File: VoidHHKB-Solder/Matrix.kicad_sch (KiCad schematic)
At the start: 136 parts

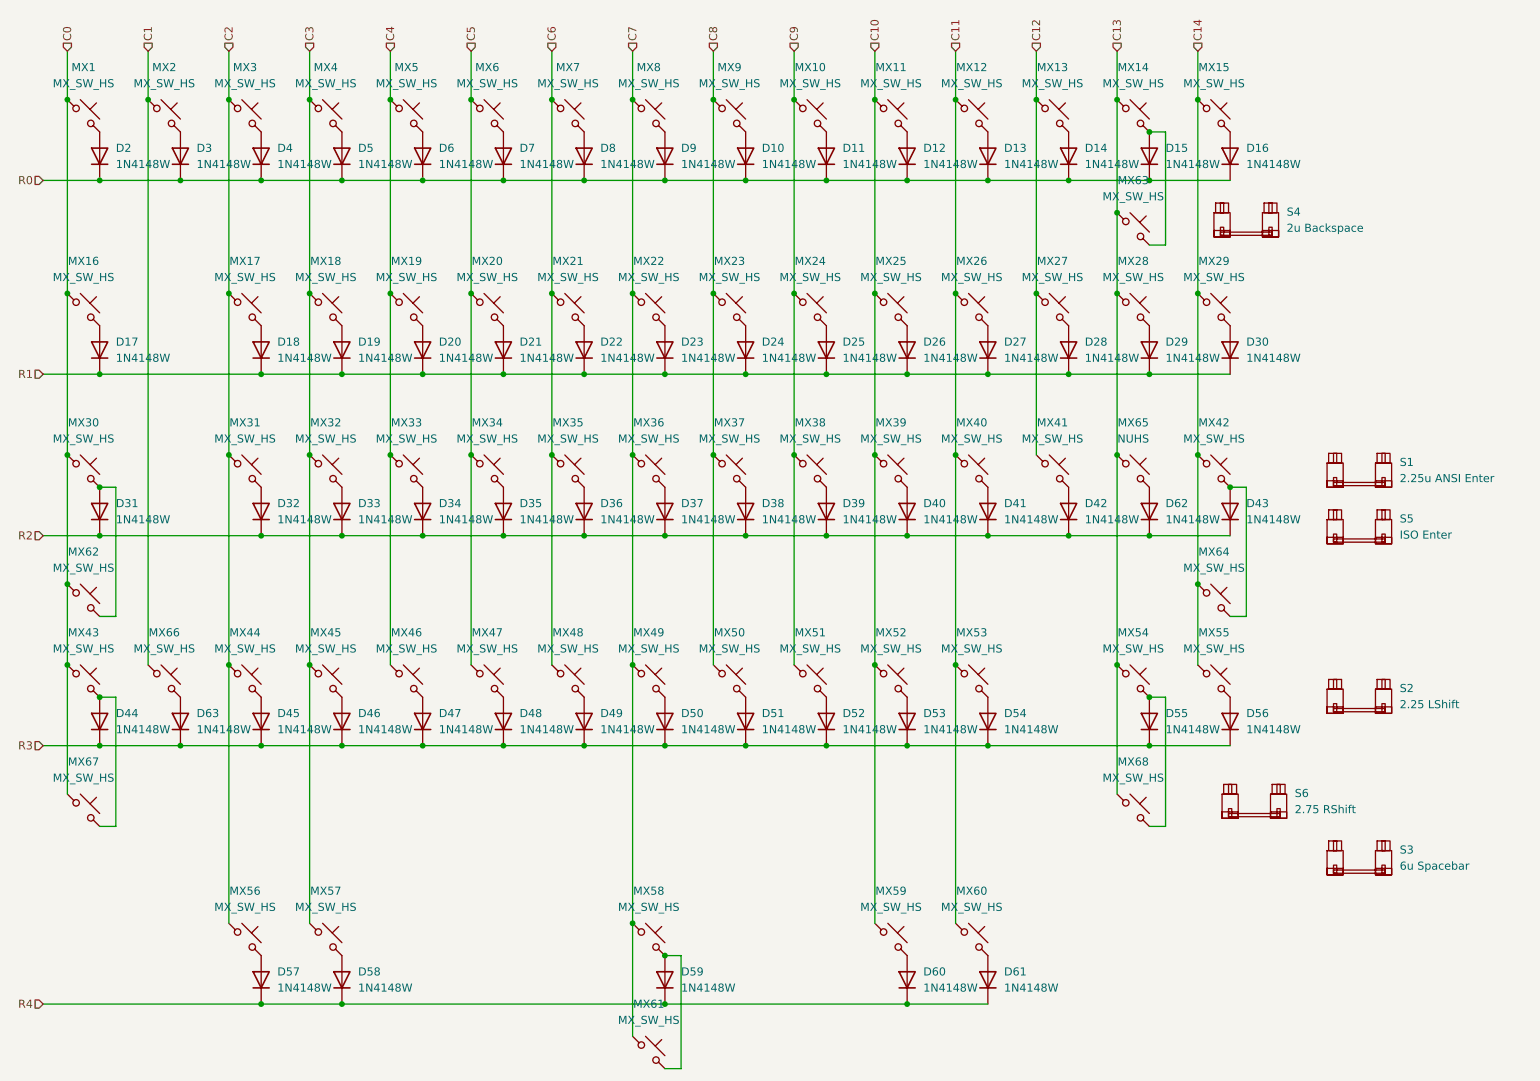
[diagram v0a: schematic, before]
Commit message: Updated Solder PCB. Fix designators and add labels to silk screen.
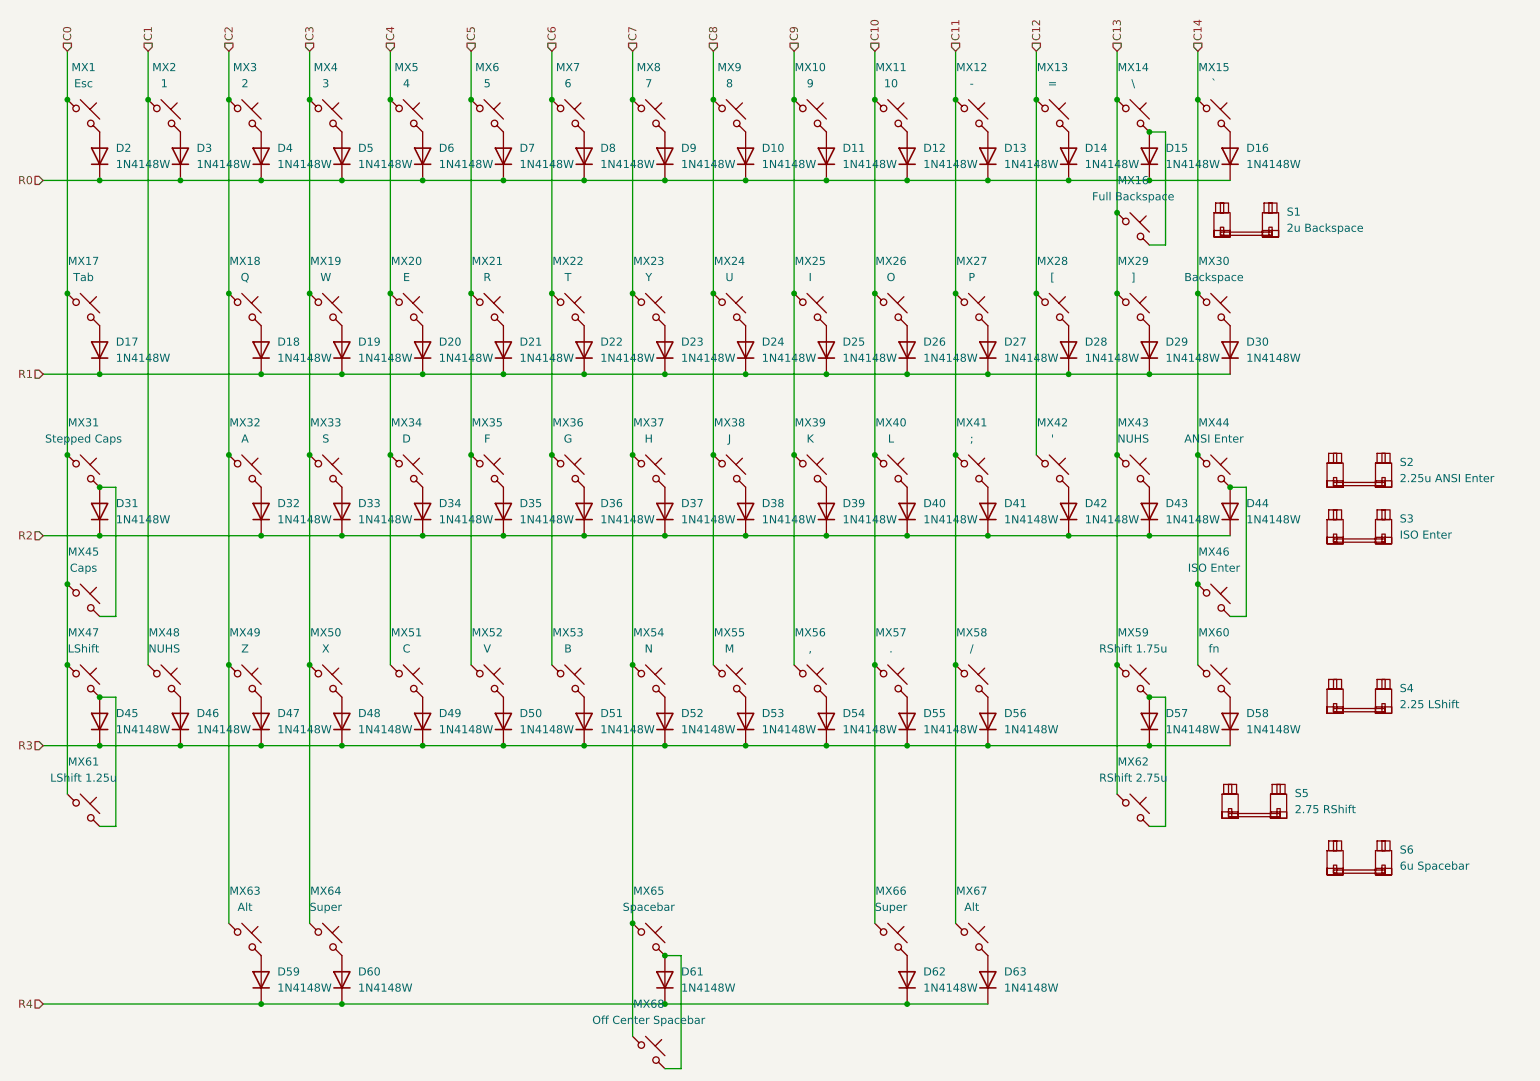
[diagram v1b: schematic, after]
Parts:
- MX1: value MX_SW_HS -> Esc
- MX10: value MX_SW_HS -> 9
- MX11: value MX_SW_HS -> 10
- MX12: value MX_SW_HS -> -
- MX13: value MX_SW_HS -> =
- MX14: value MX_SW_HS -> \
- MX15: value MX_SW_HS -> `
- MX16: renamed from MX63; value MX_SW_HS -> Full Backspace
- MX17: renamed from MX16; value MX_SW_HS -> Tab; footprint PCM_marbastlib-mx:SW_MX_1u -> PCM_marbastlib-mx:SW_MX_1.5u
- MX18: renamed from MX17; value MX_SW_HS -> Q
- MX19: renamed from MX18; value MX_SW_HS -> W
- MX2: value MX_SW_HS -> 1
- MX20: renamed from MX19; value MX_SW_HS -> E
- MX21: renamed from MX20; value MX_SW_HS -> R
- MX22: renamed from MX21; value MX_SW_HS -> T
- MX23: renamed from MX22; value MX_SW_HS -> Y
- MX24: renamed from MX23; value MX_SW_HS -> U
- MX25: renamed from MX24; value MX_SW_HS -> I
- MX26: renamed from MX25; value MX_SW_HS -> O
- MX27: renamed from MX26; value MX_SW_HS -> P
- MX28: renamed from MX27; value MX_SW_HS -> [
- MX29: renamed from MX28; value MX_SW_HS -> ]
- MX3: value MX_SW_HS -> 2
- MX30: renamed from MX29; value MX_SW_HS -> Backspace; footprint PCM_marbastlib-mx:SW_MX_1u -> PCM_marbastlib-mx:SW_MX_1.5u
- MX31: renamed from MX30; value MX_SW_HS -> Stepped Caps
- MX32: renamed from MX31; value MX_SW_HS -> A
- MX33: renamed from MX32; value MX_SW_HS -> S
- MX34: renamed from MX33; value MX_SW_HS -> D
- MX35: renamed from MX34; value MX_SW_HS -> F
- MX36: renamed from MX35; value MX_SW_HS -> G
- MX37: renamed from MX36; value MX_SW_HS -> H
- MX38: renamed from MX37; value MX_SW_HS -> J
- MX39: renamed from MX38; value MX_SW_HS -> K
- MX4: value MX_SW_HS -> 3
- MX40: renamed from MX39; value MX_SW_HS -> L
- MX41: renamed from MX40; value MX_SW_HS -> ;
- MX42: renamed from MX41; value MX_SW_HS -> '
- MX44: renamed from MX42; value MX_SW_HS -> ANSI Enter
- MX45: renamed from MX62; value MX_SW_HS -> Caps
- MX46: renamed from MX64; value MX_SW_HS -> ISO Enter
- MX47: renamed from MX43; value MX_SW_HS -> LShift
- MX48: renamed from MX66; value MX_SW_HS -> NUHS
- MX49: renamed from MX44; value MX_SW_HS -> Z
- MX5: value MX_SW_HS -> 4
- MX50: renamed from MX45; value MX_SW_HS -> X
- MX51: renamed from MX46; value MX_SW_HS -> C
- MX52: renamed from MX47; value MX_SW_HS -> V
- MX53: renamed from MX48; value MX_SW_HS -> B
- MX54: renamed from MX49; value MX_SW_HS -> N
- MX55: renamed from MX50; value MX_SW_HS -> M
- MX56: renamed from MX51; value MX_SW_HS -> ,
- MX57: renamed from MX52; value MX_SW_HS -> .
- MX58: renamed from MX53; value MX_SW_HS -> /
- MX59: renamed from MX54; value MX_SW_HS -> RShift 1.75u; footprint PCM_marbastlib-mx:SW_MX_1u -> PCM_marbastlib-mx:SW_MX_1.75u
- MX6: value MX_SW_HS -> 5
- MX60: renamed from MX55; value MX_SW_HS -> fn
- MX61: renamed from MX67; value MX_SW_HS -> LShift 1.25u; footprint PCM_marbastlib-mx:SW_MX_1u -> PCM_marbastlib-mx:SW_MX_1.25u
- MX62: renamed from MX68; value MX_SW_HS -> RShift 2.75u
- MX63: renamed from MX56; value MX_SW_HS -> Alt
- MX64: renamed from MX57; value MX_SW_HS -> Super; footprint PCM_marbastlib-mx:SW_MX_1u -> PCM_marbastlib-mx:SW_MX_1.5u
- MX65: renamed from MX58; value MX_SW_HS -> Spacebar
- MX66: renamed from MX59; value MX_SW_HS -> Super; footprint PCM_marbastlib-mx:SW_MX_1u -> PCM_marbastlib-mx:SW_MX_1.5u
- MX67: renamed from MX60; value MX_SW_HS -> Alt
- MX68: renamed from MX61; value MX_SW_HS -> Off Center Spacebar
- MX7: value MX_SW_HS -> 6
- MX8: value MX_SW_HS -> 7
- MX9: value MX_SW_HS -> 8
- renumbered D62 to D43, D43 to D44, D44 to D45, D63 to D46, D45 to D47, D46 to D48, D47 to D49, D48 to D50, D49 to D51, D50 to D52, D51 to D53, D52 to D54, D53 to D55, D54 to D56, D55 to D57, D56 to D58, D57 to D59, D58 to D60, D59 to D61, D60 to D62, D61 to D63, MX65 to MX43, S4 to S1, S1 to S2, S5 to S3, S2 to S4, S6 to S5, S3 to S6
